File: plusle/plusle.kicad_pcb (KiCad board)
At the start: 2 copper layers, 97 x 31 mm, 7 parts, among them J1 Battery, J2 MotorA, J3 MotorB, SW1 SW_SPST, U1 ESP32-DEVKIT-V1, U2 ROB-14450

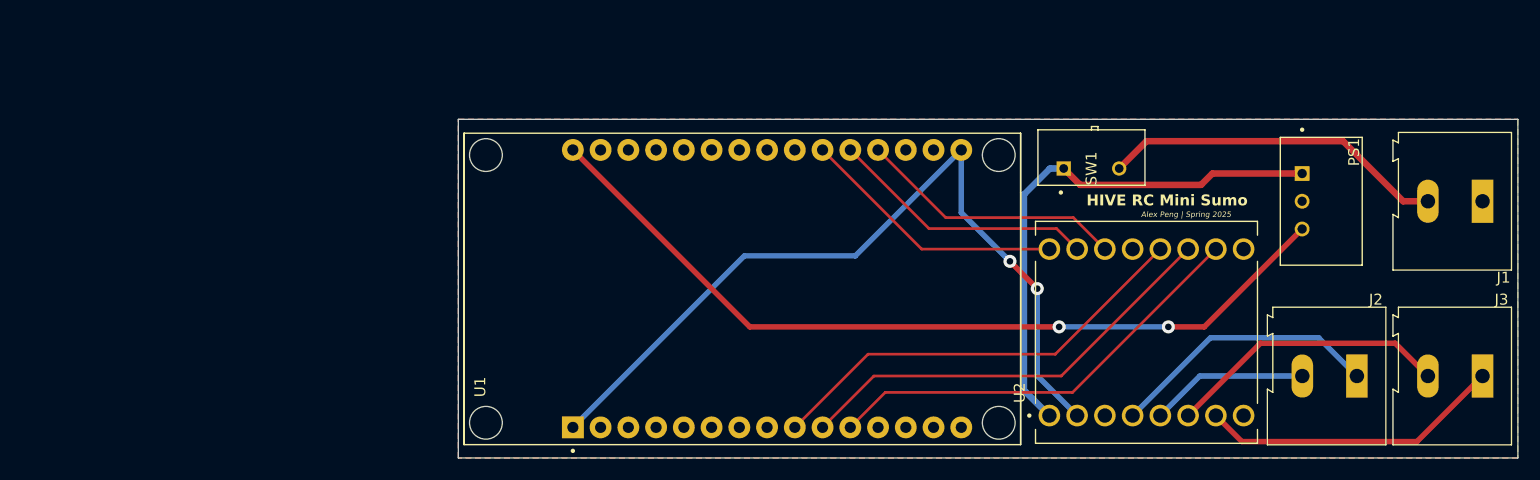
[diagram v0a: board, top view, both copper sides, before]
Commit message: updated
updated layout and schematic for hive bot (powered by 9v battery with switch)
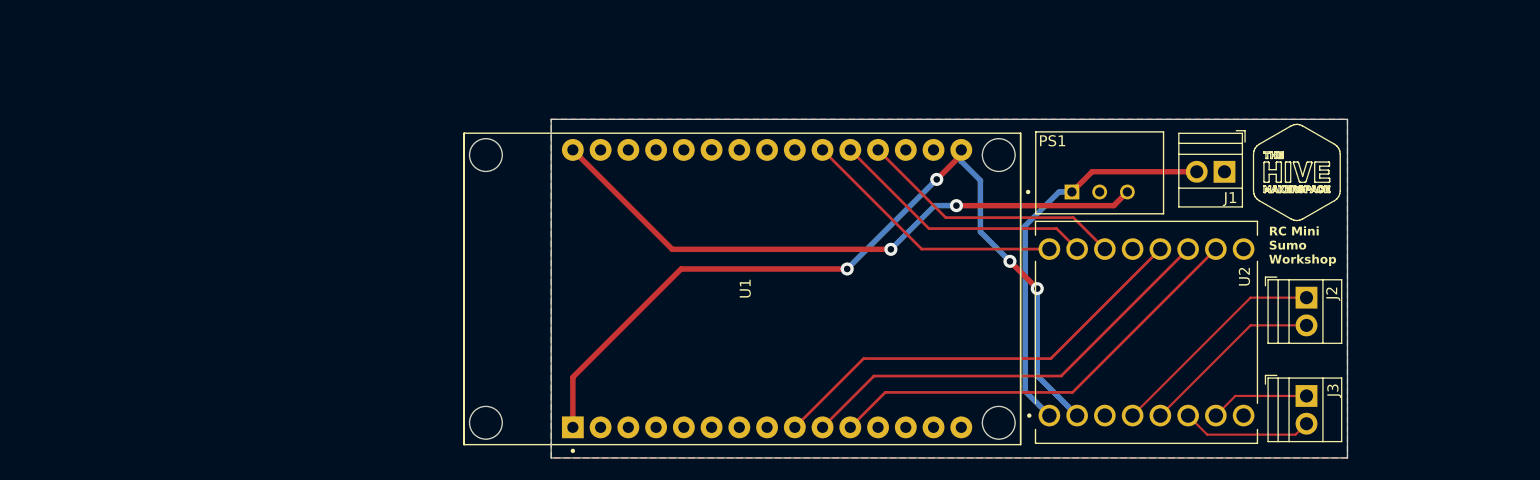
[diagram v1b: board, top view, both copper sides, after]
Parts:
- removed SW1: SW_SPST, Button_Switch_THT:SW_AS11CP
- J1, J2, J3: footprint TerminalBlock:TerminalBlock_Altech_AK300-2_P5.00mm -> TerminalBlock:TerminalBlock_Xinya_XY308-2.54-2P_1x02_P2.54mm_Horizontal
- moved J1 23.8 mm to (133.1, 40.3)
- moved PS1 20.5 mm to (121.7, 40.4), turned to 0 degrees
- moved J3 16.2 mm to (140.7, 60.8), turned to -90 degrees
- moved J2 8.53 mm to (140.7, 51.8), turned to -90 degrees
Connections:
- J1 pad 2: Net-(J1-Pin_2) -> +12V
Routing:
- net Net-(J1-Pin_2): track 31.6 -> 0.00 mm
- net +5V: track 77.2 -> 56.7 mm
- net Net-(J3-Pin_1): track 27.9 -> 9.04 mm
- net Net-(J3-Pin_2): track 25.9 -> 12.0 mm
- net +12V: track 48.7 -> 36.0 mm
- net Net-(J2-Pin_1): track 24.9 -> 20.4 mm
- net +3.3V: track 74.8 -> 77.7 mm, vias 2 -> 4
- net Net-(J2-Pin_2): track 14.5 -> 16.8 mm
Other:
- board size 97 x 31 mm -> 72.9 x 31 mm
- board text added: "Alex Peng Spring 2025 lunoxrobotics.com"
- board text added: "RC Mini Sumo Workshop"
- board text removed: "Alex Peng | Spring 2025"
- board text removed: "HIVE RC Mini Sumo"

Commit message: NewIteration
new compact board for personal plusle project, non-hive
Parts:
- removed PS1: TSR_1-2450, TSR_1-2433:CONV_TSR_1-2433
- removed U1: ESP32-DEVKIT-V1, Library:MODULE_ESP32_DEVKIT_V1
- removed U2: ROB-14450, Library:MODULE_ROB-14450
- added A1: Arduino_Nano_v3.x, Module:Arduino_Nano, F.Cu at (65.1, 28.2)
- added C1: 0.1uf, Capacitor_SMD:C_0805_2012Metric_Pad1.18x1.45mm_HandSolder, F.Cu at (63.9, 33.4)
- added C2: 0.1uf, Capacitor_SMD:C_0805_2012Metric_Pad1.18x1.45mm_HandSolder, F.Cu at (63.9, 36.7)
- added C3: 0.1uf, Capacitor_SMD:C_0805_2012Metric_Pad1.18x1.45mm_HandSolder, F.Cu at (63.9, 40.0)
- added C4: 0.1uf, Capacitor_SMD:C_0805_2012Metric_Pad1.18x1.45mm_HandSolder, B.Cu at (52.9, 39.8)
- added C5: 0.1uf, Capacitor_SMD:C_0805_2012Metric_Pad1.18x1.45mm_HandSolder, B.Cu at (52.9, 36.5)
- added C6: 0.1uf, Capacitor_SMD:C_0805_2012Metric_Pad1.18x1.45mm_HandSolder, B.Cu at (52.9, 33.2)
- added C7: 0.1uf, Capacitor_SMD:C_0805_2012Metric_Pad1.18x1.45mm_HandSolder, F.Cu at (28.4, 36.5)
- added C8: 0.1uf, Capacitor_SMD:C_0805_2012Metric_Pad1.18x1.45mm_HandSolder, F.Cu at (41.1, 36.5)
- added D1: GREEN, Capacitor_SMD:C_0603_1608Metric_Pad1.08x0.95mm_HandSolder, F.Cu at (80.2, 35.1)
- added D2: GREEN, Capacitor_SMD:C_0603_1608Metric_Pad1.08x0.95mm_HandSolder, F.Cu at (80.2, 38.3)
- added F1: 15A, Fuse:Fuse_1206_3216Metric_Pad1.42x1.75mm_HandSolder, F.Cu at (71.7, 36.4)
- added G***: LOGO, LOGO, F.Cu at (52.4, 35.5)
- added H1: MountingHole, MountingHole:MountingHole_2.2mm_M2_ISO7380, F.Cu at (27.8, 46.6)
- added H2: MountingHole, MountingHole:MountingHole_2.2mm_M2_ISO7380, F.Cu at (67.3, 46.6)
- added J4: Receiver Connection1, Connector_PinHeader_2.54mm:PinHeader_1x03_P2.54mm_Vertical, F.Cu at (44.7, 46.9)
- added J5: Battery, Connector_AMASS:AMASS_XT30PW-M_1x02_P2.50mm_Horizontal, B.Cu at (58.0, 35.0)
- added R1: 15k, Resistor_SMD:R_0805_2012Metric_Pad1.20x1.40mm_HandSolder, F.Cu at (28.4, 31.9)
- added R2: 15k, Resistor_SMD:R_0805_2012Metric_Pad1.20x1.40mm_HandSolder, F.Cu at (41.1, 31.9)
- added R3: 600, Diode_SMD:D_0805_2012Metric_Pad1.15x1.40mm_HandSolder, F.Cu at (75.7, 34.8)
- added R4: 600, Diode_SMD:D_0805_2012Metric_Pad1.15x1.40mm_HandSolder, F.Cu at (75.8, 38.1)
- added SW1: SW_SPST, Button_Switch_THT:SW_AS11CP, F.Cu at (75.5, 30.1)
- added U3: DRV8871DDA, Package_SO:Texas_HTSOP-8-1EP_3.9x4.9mm_P1.27mm_EP2.95x4.9mm_Mask2.4x3.1mm_ThermalVias, F.Cu at (33.4, 34.2)
- added U4: DRV8871DDA, Package_SO:Texas_HTSOP-8-1EP_3.9x4.9mm_P1.27mm_EP2.95x4.9mm_Mask2.4x3.1mm_ThermalVias, F.Cu at (46.1, 34.2)
- J1: value Battery -> Receiver Connection2; footprint TerminalBlock:TerminalBlock_Xinya_XY308-2.54-2P_1x02_P2.54mm_Horizontal -> Connector_PinHeader_2.54mm:PinHeader_1x03_P2.54mm_Vertical
- moved J1 84.7 mm to (48.7, 46.9), turned to 90 degrees
- moved J2 67.1 mm to (73.9, 44.8), turned to 180 degrees
- moved J3 62.2 mm to (80.6, 44.8), turned to 180 degrees
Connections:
- J1 pad 1: GND -> RCSignalB
- J1 pad 2: +12V -> Arduino5V
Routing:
- net +3.3V: track 77.7 -> 0.00 mm, vias 4 -> 0
- net ArduinoVIN: track 0.00 -> 70.0 mm, vias 0 -> 5
- net Arduino5V: track 0.00 -> 67.5 mm
- net +5V: track 56.7 -> 0.00 mm, vias 2 -> 0
- net GND: track 0.00 -> 56.0 mm, vias 0 -> 11
- net PWMB: track 40.2 -> 0.00 mm
- net Net-(J3-Pin_1): track 9.04 -> 48.1 mm, vias 0 -> 1
- net BIn2: track 40.2 -> 3.47 mm
- net BIn1: track 40.2 -> 3.48 mm
- net Net-(J3-Pin_2): track 12.0 -> 48.1 mm, vias 0 -> 1
- net +12V: track 36.0 -> 0.00 mm
- net Net-(J2-Pin_1): track 20.4 -> 52.9 mm, vias 0 -> 1
- net Net-(J2-Pin_2): track 16.8 -> 47.2 mm, vias 0 -> 1
- net PWMA: track 24.5 -> 0.00 mm
- net Net-(J5-Pin_2): track 0.00 -> 22.4 mm, vias 0 -> 1
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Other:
- board size 72.9 x 31 mm -> 57 x 22 mm
- board text added: "Alex Peng lunoxrobotics.com"
- board text added: "Plusle RC Mini Sumo"
- board text removed: "Alex Peng Spring 2025 lunoxrobotics.com"
- board text removed: "RC Mini Sumo Workshop"
